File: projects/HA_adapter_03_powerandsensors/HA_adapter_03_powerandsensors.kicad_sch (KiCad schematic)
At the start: 13 parts, among them J1 TerminalBlock_2pin, J2 TerminalBlock_2pin, J3 TerminalBlock_3pin, J4 TerminalBlock_2pin, J5 TerminalBlock_3pin, J6 TerminalBlock_3pin, J7 TerminalBlock_3pin, J8 TerminalBlock_3pin, J9 TerminalBlock_3pin, T1 HA_adapter_03_powerandsensors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

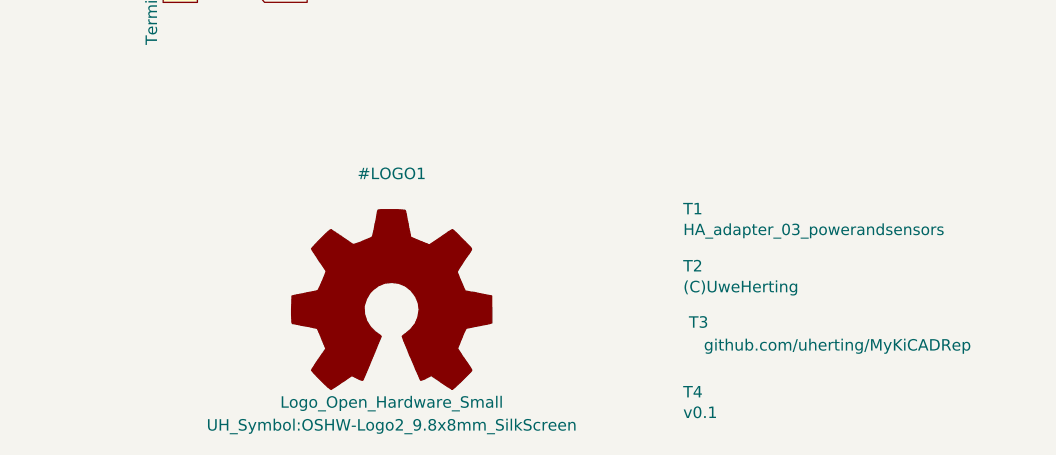
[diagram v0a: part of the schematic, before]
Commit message: snapshot prior to changing HA_ESP8266_01 (removing 3pin for one IO and adding 4k7 for dallas 18b20 sensor)
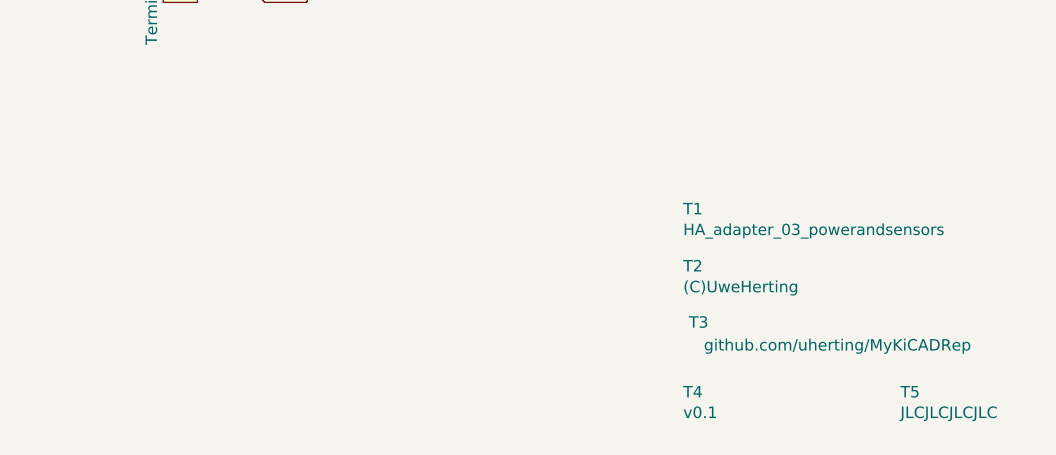
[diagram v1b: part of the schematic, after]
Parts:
- added T5: JLCJLCJLCJLC, UH_HA:PCB_Version, symbol UH_HA:PCB_Version
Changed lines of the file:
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@@
+    )
+  )
+  (symbol (lib_id "UH_HA:PCB_Version") (at 255.27 160.02 0) (unit 1)
+    (in_bom yes) (on_board yes)
+    (property "Reference" "T5" (id 0) (at 255.905 158.877 0)
+      (effects (font (size 1.27 1.27)) (justify left))
+    )
+    (property "Value" "JLCJLCJLCJLC" (id 1) (at 255.905 161.163 0)
+      (effects (font (size 1.27 1.27)) (justify left))
+    )
+    (property "Footprint" "UH_HA:PCB_Version" (id 2) (at 256.54 165.1 0)
+      (effects (font (size 1.27 1.27)) hide)
+    )
+    (property "Datasheet" "" (id 3) (at 255.27 160.02 0)
+      (effects (font (size 1.27 1.27)) hide)
     )
   )
@@
     (pin "3")
   )
-  (symbol (lib_id "UH_Graphic:Logo_Open_Hardware_Small") (at 199.39 149.86 0) (unit 1)
-    (in_bom yes) (on_board yes)
-    (property "Reference" "#LOGO1" (id 0) (at 199.39 134.62 0))
-    (property "Value" "Logo_Open_Hardware_Small" (id 1) (at 199.39 160.02 0))
-    (property "Footprint" "UH_Symbol:OSHW-Logo2_9.8x8mm_SilkScreen" (id 2) (at 199.39 162.56 0))
-    (property "Datasheet" "~" (id 3) (at 199.39 149.86 0)
-      (effects (font (size 1.27 1.27)) hide)
-    )
-  )
   (sheet_instances
     (path "/" (page "1"))
@@
       (reference "#FLG04") (unit 1) (value "PWR_FLAG") (footprint "")
     )
-    (path "/abc7a922-4dbd-4232-9da1-38d10da220c8"
-      (reference "#LOGO1") (unit 1) (value "Logo_Open_Hardware_Small") (footprint "UH_Symbol:OSHW-Logo2_9.8x8mm_SilkScreen")
-    )
     (path "/28a026e3-64cd-43b6-9e55-fdae3c6beb3a"
       (reference "#PWR01") (unit 1) (value "+5V") (footprint "")
@@
       (reference "T4") (unit 1) (value "v0.1") (footprint "UH_HA:PCB_Version")
     )
-  )
+    (path "/d17f14bc-b059-4517-90aa-44b3764a41be"
+      (reference "T5") (unit 1) (value "JLCJLCJLCJLC") (footprint "UH_HA:PCB_Version")
+    )
+  )
